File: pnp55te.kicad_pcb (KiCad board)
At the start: 2 copper layers, 154 x 109 mm, 59 parts, among them U1 TPIC8101, U3 molex_48pin_MRE, X1 55pin_january_5.1

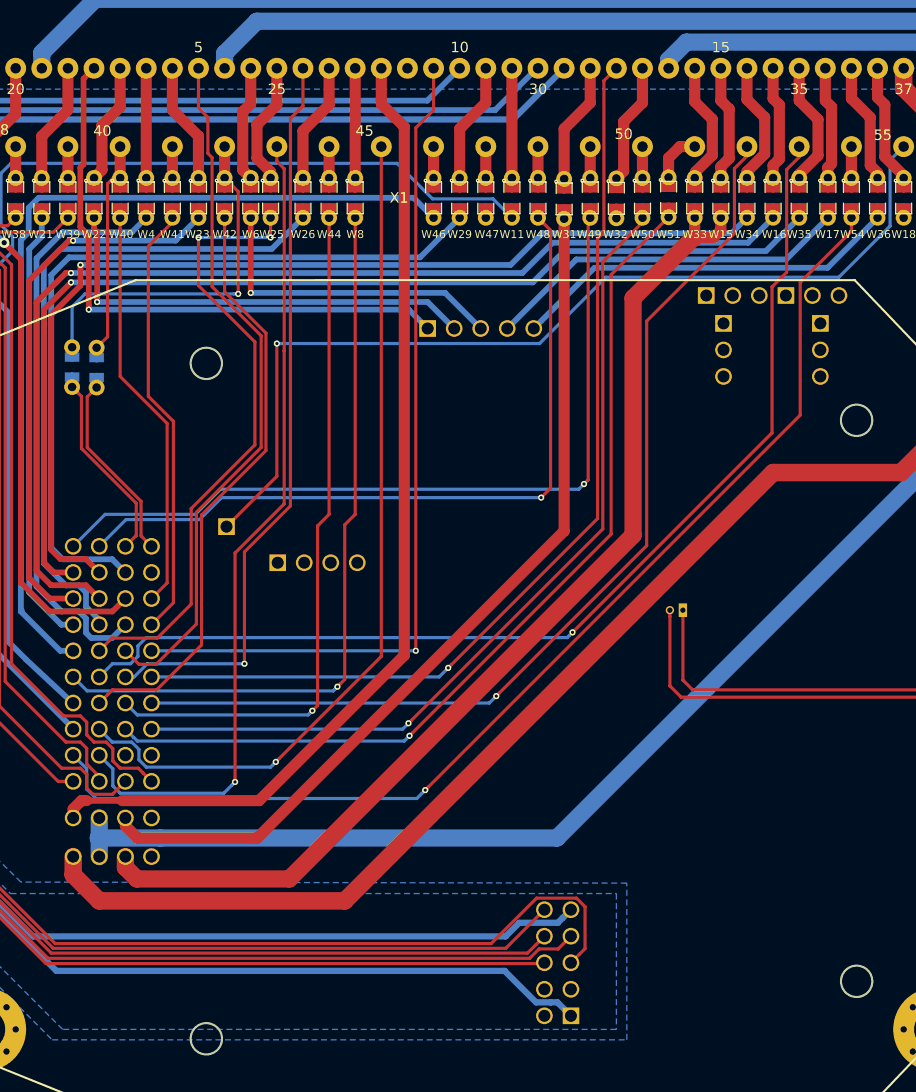
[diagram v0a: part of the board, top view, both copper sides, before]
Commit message: Add holes for caps on bottom of MRE (#5)
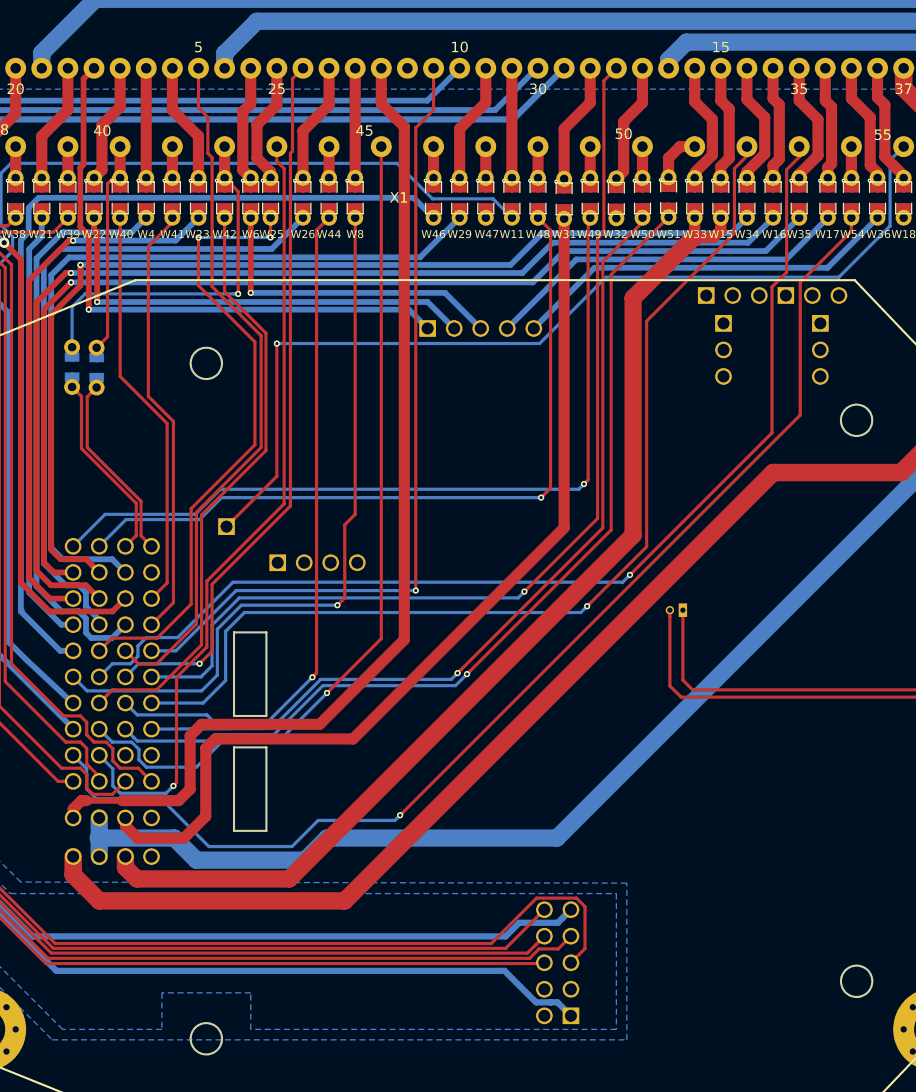
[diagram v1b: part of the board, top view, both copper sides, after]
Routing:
- net /ECO_OUT: track 108.6 -> 112.4 mm
- net /RESERVED_HI_CUR: track 85.3 -> 89.0 mm
- net /AFR_NARROW: track 81.8 -> 78.4 mm
- net /TACH: track 79.0 -> 75.7 mm
- net /RESERVED_AIN2: track 95.8 -> 98.6 mm
- net /MAF: track 71.2 -> 68.7 mm
- net /L_LINE: track 92.8 -> 95.1 mm
- net /12_IGN_KEY: track 95.8 -> 97.9 mm
- net /CAM_HALL: track 72.2 -> 70.3 mm
- net GND: track 340.7 -> 342.4 mm
- net /IAT: track 66.4 -> 65.1 mm
- net /CLT: track 82.3 -> 81.3 mm
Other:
- outline, holes or cut-outs redrawn

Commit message: fixed missing libs, misc changes.
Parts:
- U3: footprint hw_55_te:Molex_48_MRE_clean -> rusEFI_Modules:Molex_48_MRE
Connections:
- C1 pad 2: /MRE_GND -> GND
- C2 pad 2: /MRE_GND -> GND
- C5 pad 2: /MRE_GND -> GND
- C6 pad 2: /MRE_GND -> GND
- U1 pad 2: /MRE_GND -> GND
- U3 pad J809: /MRE_GND -> GND
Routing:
- net GND: track 342.4 -> 434.8 mm, vias 0 -> 60
- net /MRE_GND: track 87.6 -> 0.00 mm, vias 3 -> 0
- net /PC11_SPI3MISO: track 86.4 -> 92.3 mm
- net /PC10_SPI3SCK: track 82.3 -> 87.0 mm
- net /PC12_SPI3MOSI: track 79.5 -> 84.1 mm
- net /PB9: track 76.0 -> 80.5 mm
- net /PA15_SPI3CS: track 80.6 -> 84.7 mm
- net /AC_REQUEST: track 42.4 -> 45.2 mm
- net /RESERVED_AIN0: track 38.9 -> 40.3 mm
- net /MRE_5V: track 114.1 -> 115.3 mm
- net /RESERVED_HI_CUR: track 89.0 -> 87.9 mm
- net /AC_RELAY: track 59.3 -> 60.3 mm
- net /HI4_UNUSED: track 68.7 -> 69.6 mm
- net /CRANK_n: track 71.9 -> 72.8 mm
- net /AFR_HEATER: track 101.9 -> 101.1 mm
- added copper zone on F.Cu, net GND
- removed copper zone on B.Cu, net /MRE_GND
